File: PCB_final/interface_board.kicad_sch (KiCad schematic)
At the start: 116 parts, among them J1 02x30_Shift_Register_Connector, J2 02x30_ADC_Connector, J5 PicoPinSocketB, J6 PicoPinSocketA, U1 74HC595, U10 LM321, U2 74HC595, U3 74HC595, U4 74HC595, U5 74HC595, U6 74HC595, U7 74HC595, U8 MAX11643EEG, U9 MAX11643EEG

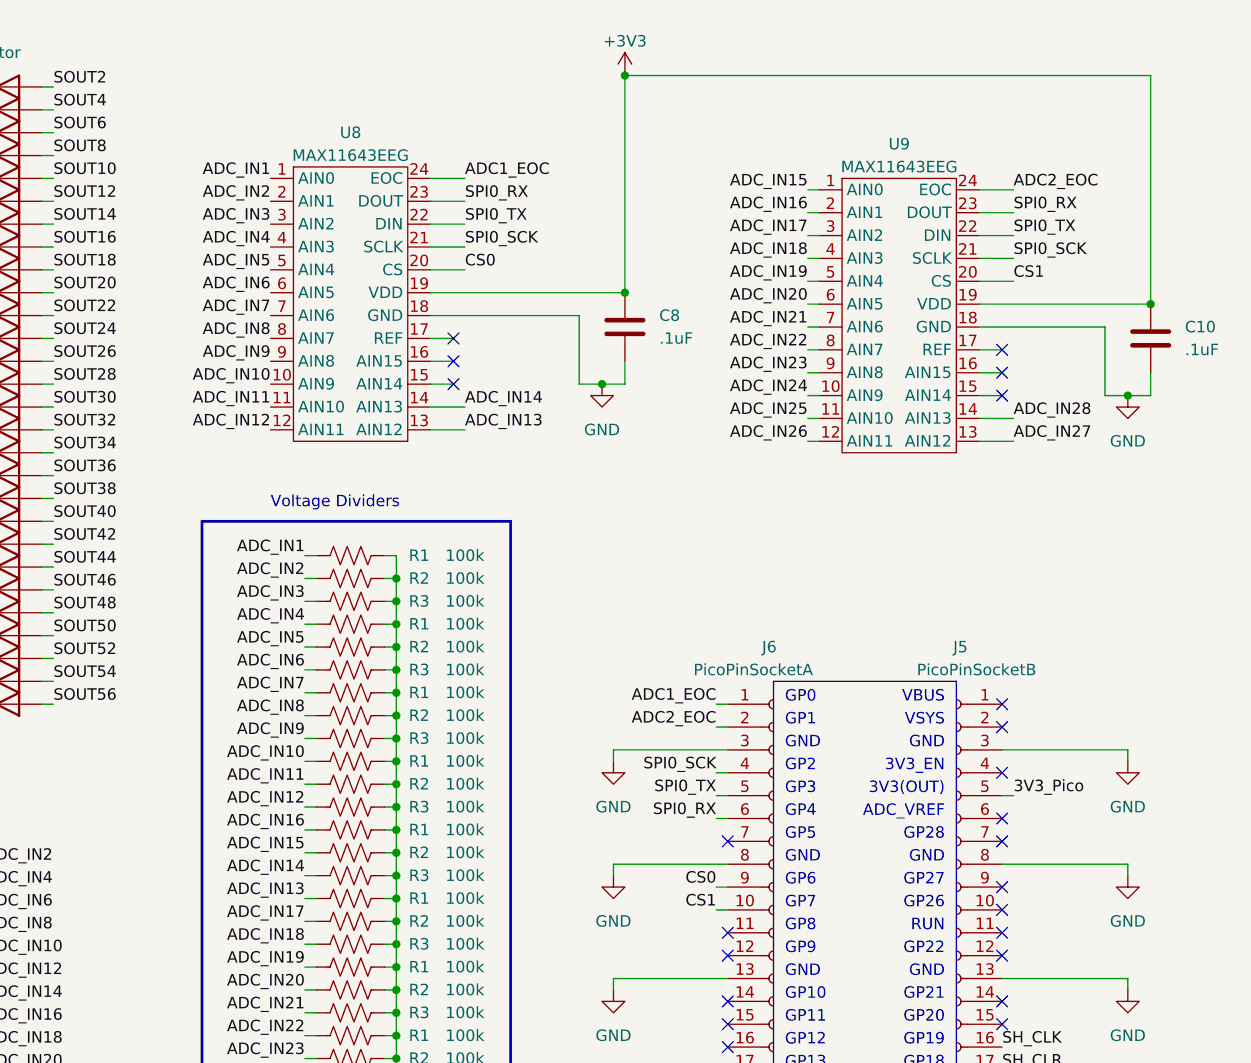
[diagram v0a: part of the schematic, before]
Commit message: PCB complete and redesigned w 4 layers. Passes desgin rule checker except for most of the silk screens. Schematic updated to connect adc unused pins to ground and beatified schematic
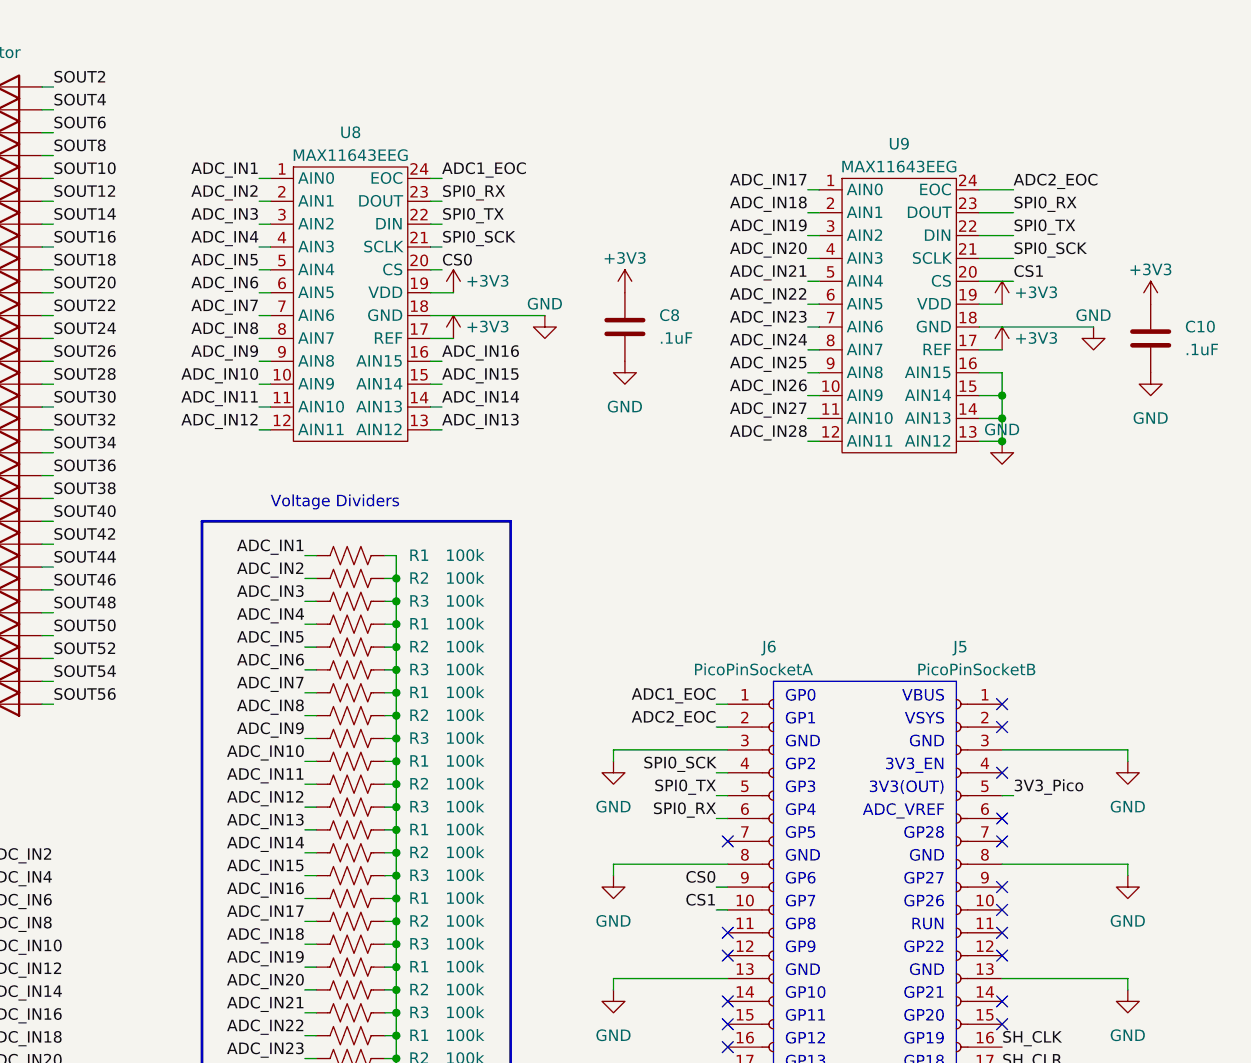
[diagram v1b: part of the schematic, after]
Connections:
- net +3V3: now also U8.17 (REF), U9.17 (REF)
- net ADC_IN13: now also R1.1; no longer R1.1
- net ADC_IN14: now also R2.1; no longer R3.1
- net ADC_IN15: now also R3.1, U8.15 (AIN14); no longer R2.1, U9.1 (AIN0)
- net ADC_IN16: now also R1.1, U8.16 (AIN15); no longer R1.1, U9.2 (AIN1)
- net ADC_IN17: now also U9.1 (AIN0); no longer U9.3 (AIN2)
- net ADC_IN18: now also U9.2 (AIN1); no longer U9.4 (AIN3)
- net ADC_IN19: now also U9.3 (AIN2); no longer U9.5 (AIN4)
- net ADC_IN20: now also U9.4 (AIN3); no longer U9.6 (AIN5)
- net ADC_IN21: now also U9.5 (AIN4); no longer U9.7 (AIN6)
- net ADC_IN22: now also U9.6 (AIN5); no longer U9.8 (AIN7)
- net ADC_IN23: now also U9.7 (AIN6); no longer U9.9 (AIN8)
- net ADC_IN24: now also U9.8 (AIN7); no longer U9.10 (AIN9)
- net ADC_IN25: now also U9.9 (AIN8); no longer U9.11 (AIN10)
- net ADC_IN26: now also U9.10 (AIN9); no longer U9.12 (AIN11)
- net ADC_IN27: now also U9.11 (AIN10); no longer U9.13 (AIN12)
- net ADC_IN28: now also U9.12 (AIN11); no longer U9.14 (AIN13)
- net GND: now also U9.13 (AIN12), U9.14 (AIN13), U9.15 (AIN14), U9.16 (AIN15)
- no-connect marks 62 -> 56

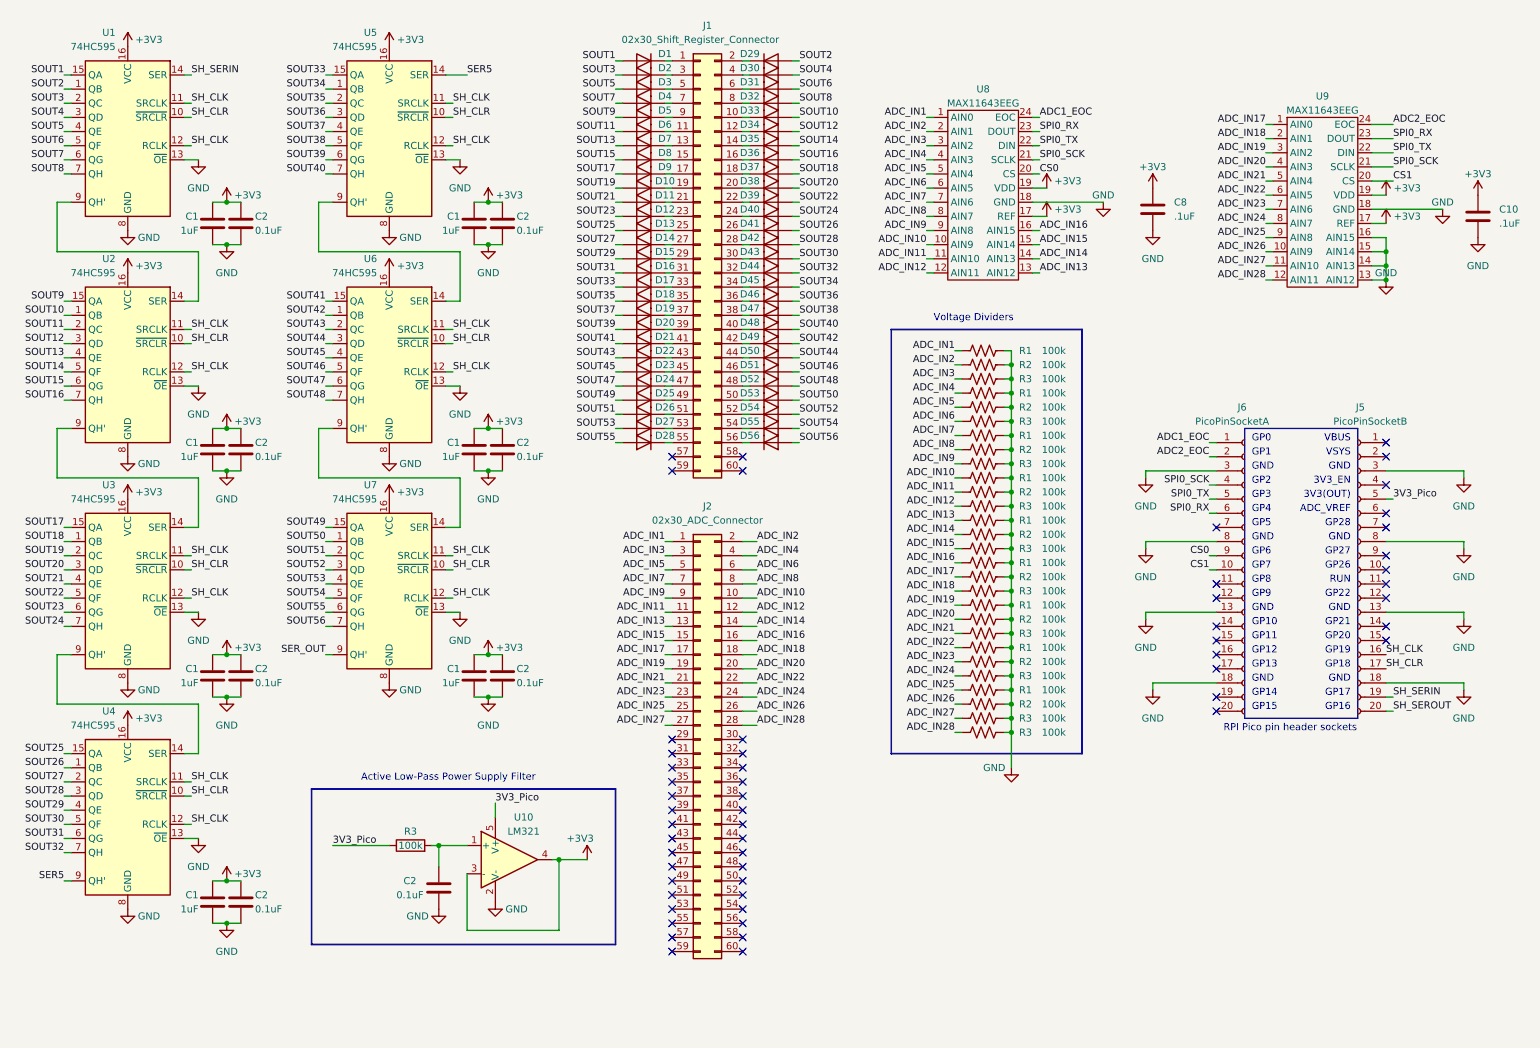
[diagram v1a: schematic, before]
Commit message: Many caps on schematic were labeled c1 and c2 incorrectly. Swapped power supply filter to Pi filter, but with no value for L yet.
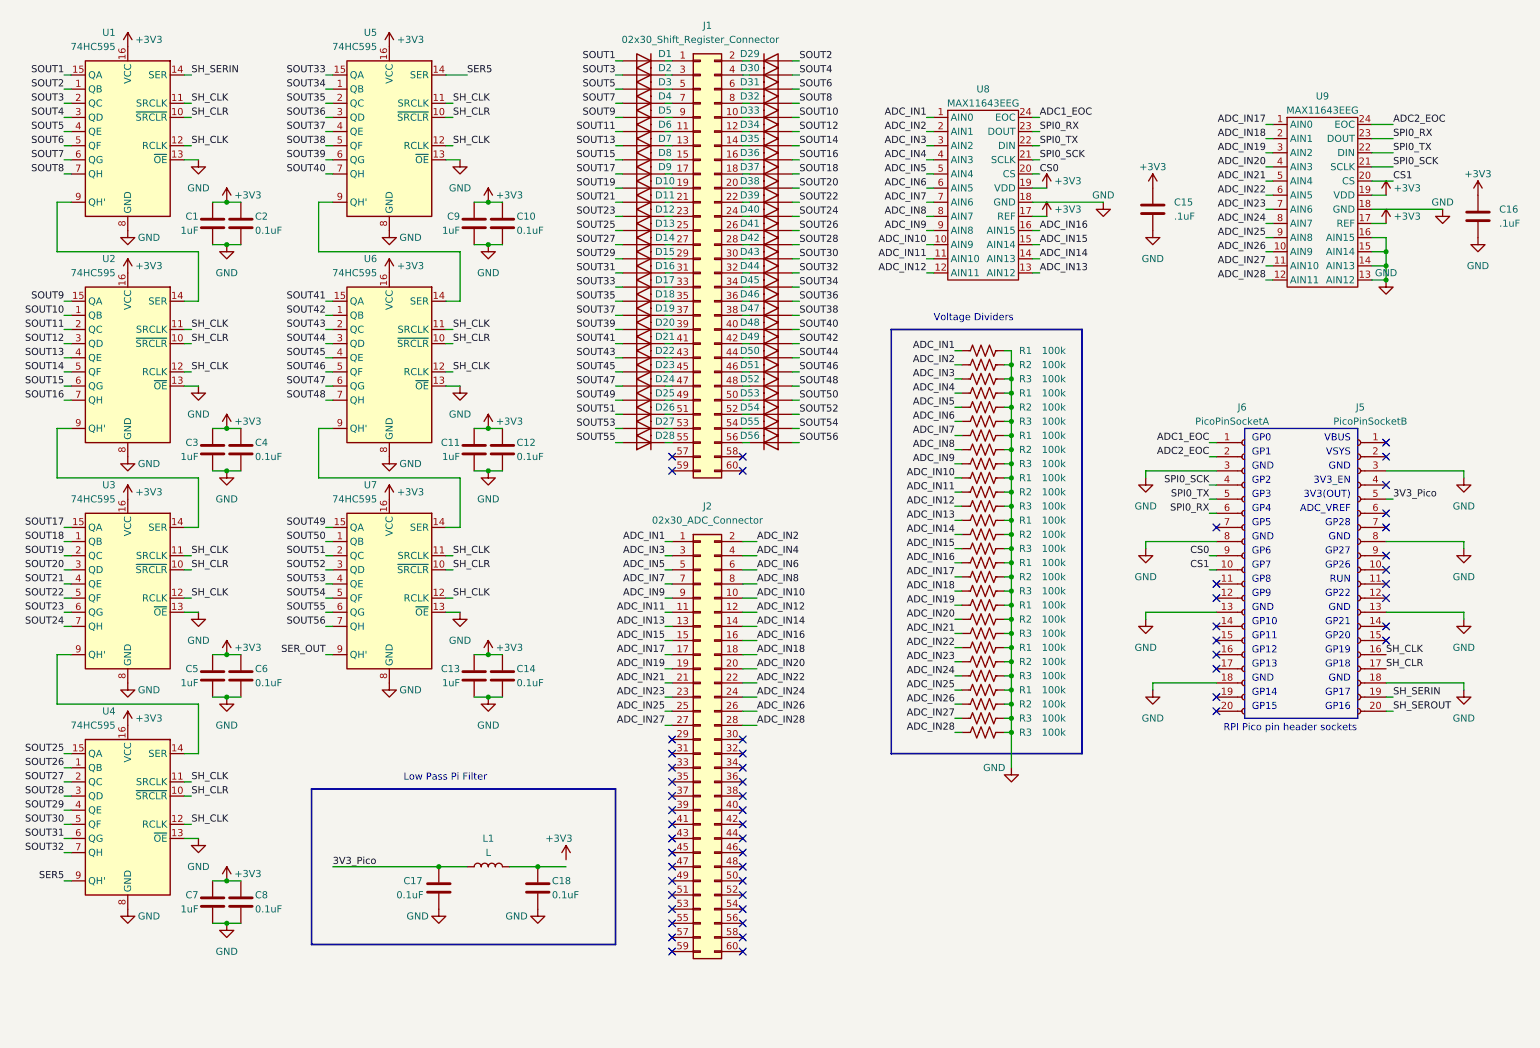
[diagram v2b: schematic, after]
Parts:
- removed R3: 100k, Resistor_SMD:R_0603_1608Metric, symbol Device:R
- removed U10: LM321, Package_TO_SOT_SMD:SOT-23-5, symbol Amplifier_Operational:LM321
- added C18: 0.1uF, Capacitor_SMD:C_0603_1608Metric, symbol Device:C
- added L1: L, symbol Device:L
- renumbered C2 to C10, C1 to C11, C2 to C12, C1 to C13, C2 to C14, C8 to C15, C10 to C16, C2 to C17, C1 to C3, C2 to C4, C1 to C5, C2 to C6, C1 to C7, C2 to C8, C1 to C9
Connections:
- net 3V3_Pico: now also C17.1, L1.1
- net GND: now also C18.2
- new net: C18.1, L1.2
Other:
- note added: "Low Pass Pi Filter"
- note removed: "Active Low-Pass Power Supply Filter"

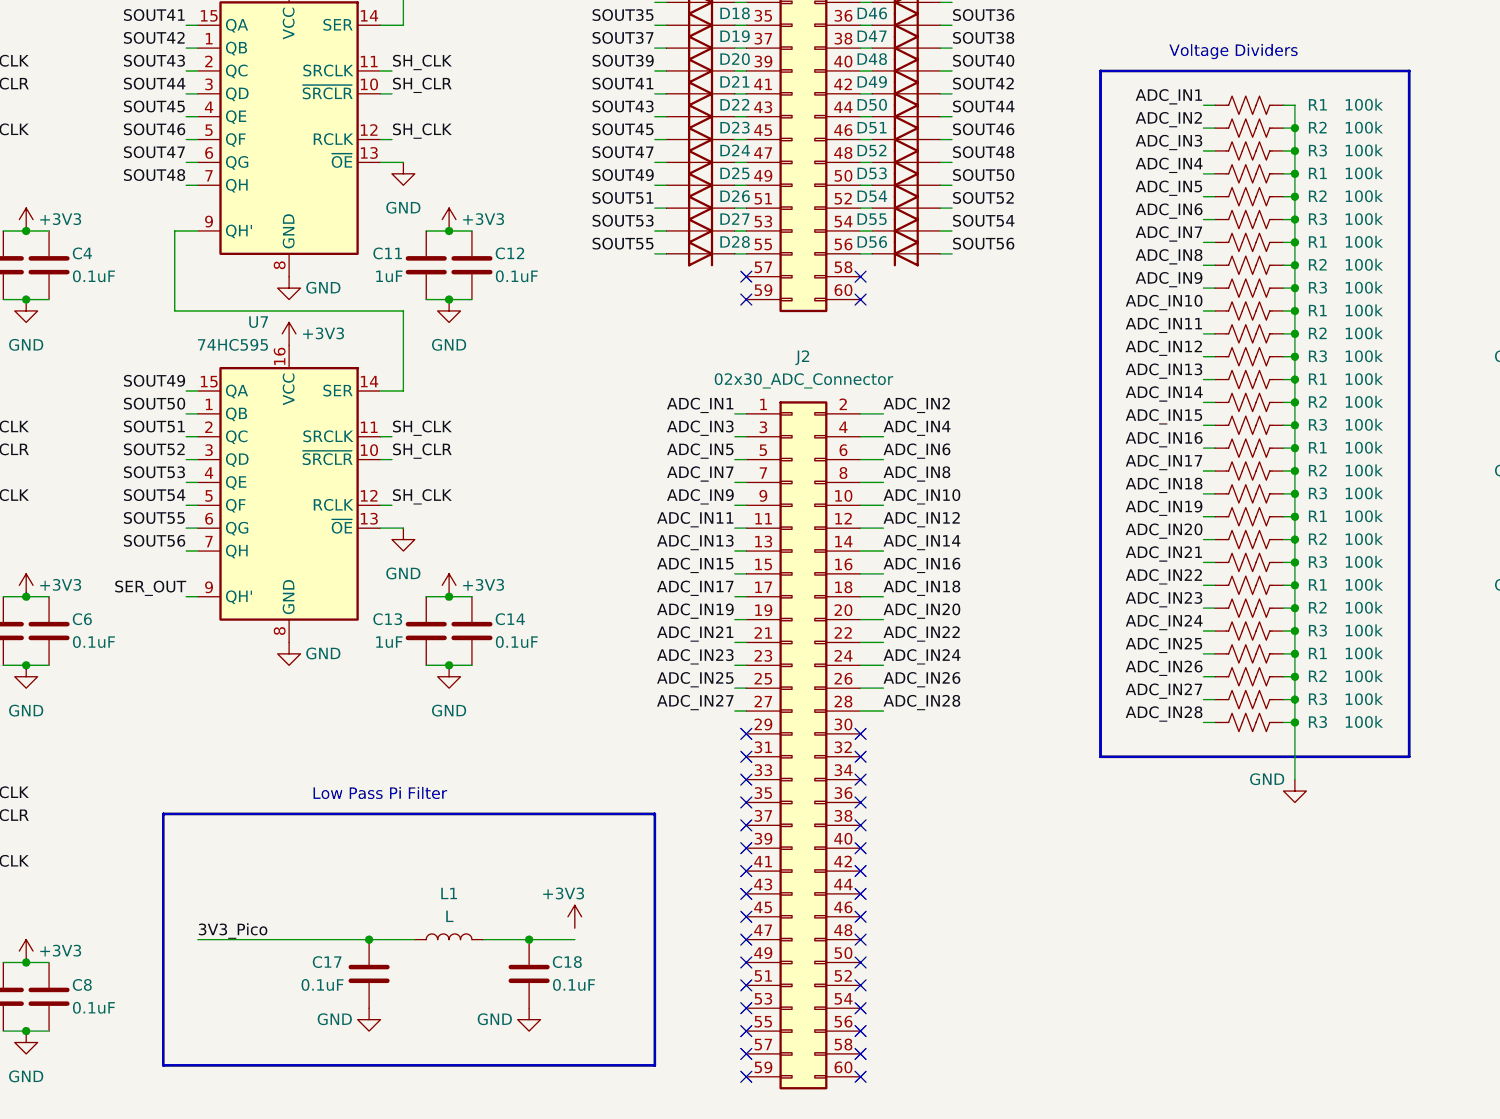
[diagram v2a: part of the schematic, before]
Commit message: Added MCP6001 as op-amp for low pass filter, fixed resistors that act as voltage dividers being named incorrectly
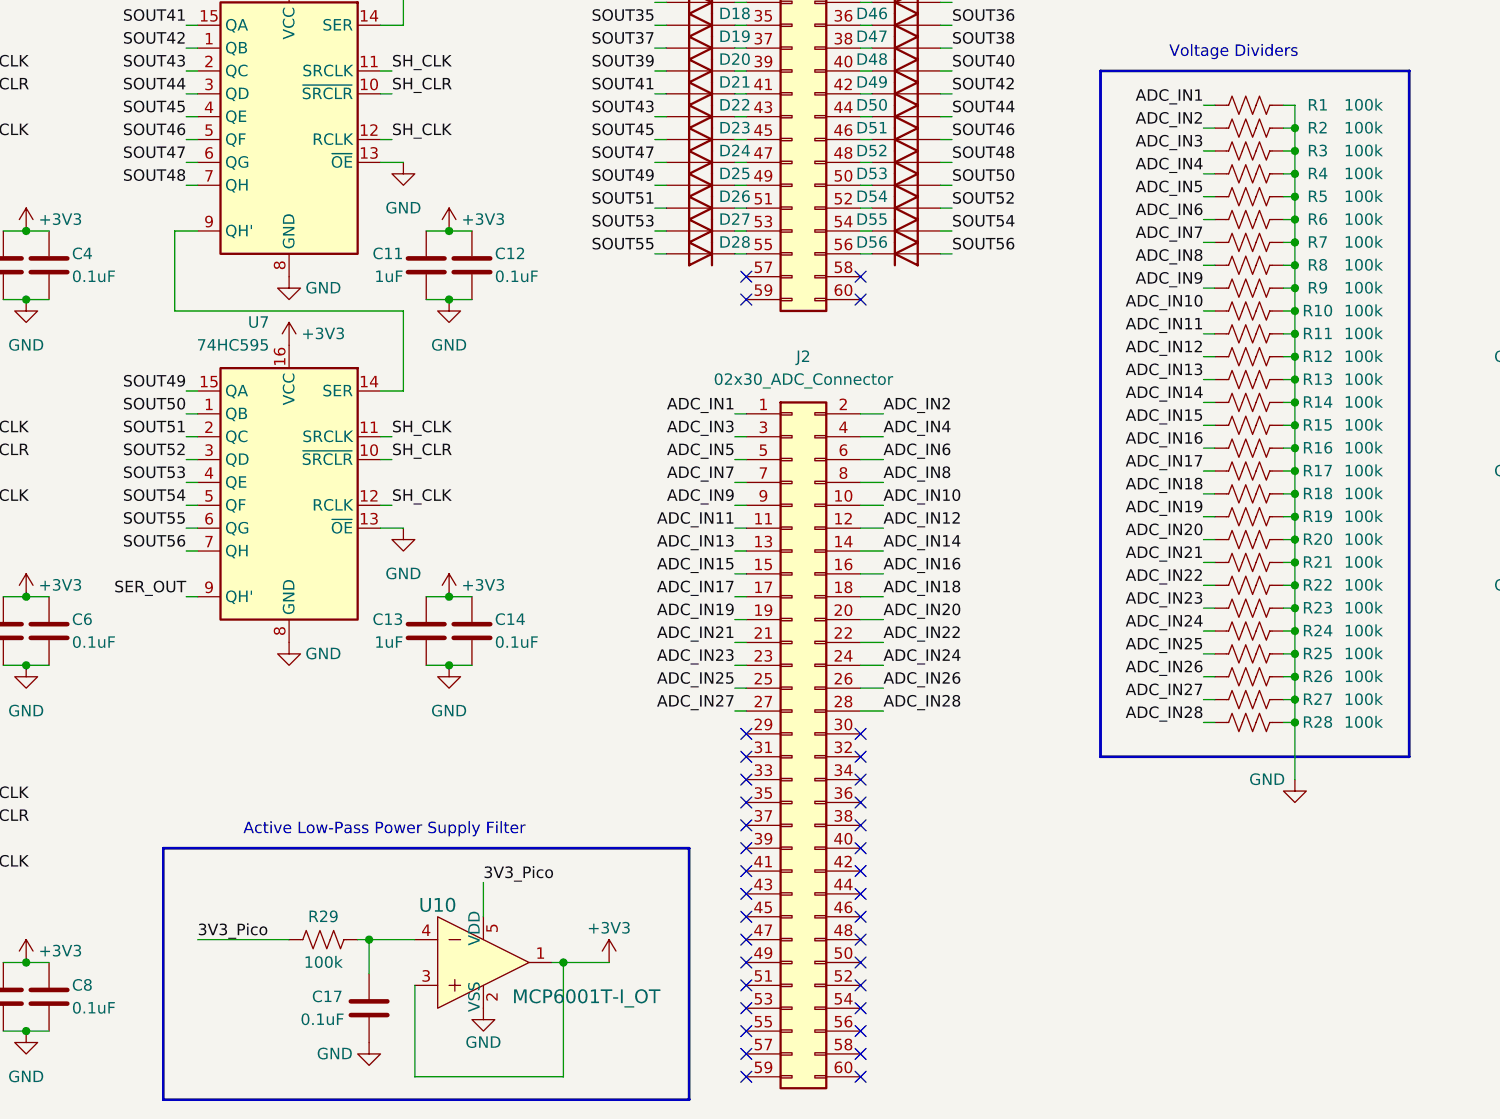
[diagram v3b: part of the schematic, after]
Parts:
- removed C18: 0.1uF, Capacitor_SMD:C_0603_1608Metric, symbol Device:C
- removed L1: L, symbol Device:L
- added R29: 100k, Resistor_SMD:R_0603_1608Metric, symbol Device:R_US
- added U10: MCP6001T-I_OT, digikey-footprints:SOT-753, symbol dk_Linear-Amplifiers-Instrumentation-OP-Amps-Buffer-Amps:MCP6001T-I_OT
- renumbered R1 to R10, R2 to R11, R3 to R12, R1 to R13, R2 to R14, R3 to R15, R1 to R16, R2 to R17, R3 to R18, R1 to R19, R2 to R20, R3 to R21, R1 to R22, R2 to R23, R3 to R24, R1 to R25, R2 to R26, R3 to R27, R3 to R28, R1 to R4, R2 to R5, R3 to R6, R1 to R7, R2 to R8, R3 to R9
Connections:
- net +3V3: now also U10.1, U10.3
- net 3V3_Pico: now also R29.1, U10.5 (VDD); no longer C17.1
- net GND: now also U10.2 (VSS)
- new net: C17.1, R29.2, U10.4
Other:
- note added: "Active Low-Pass Power Supply Filter"
- note removed: "Low Pass Pi Filter"
